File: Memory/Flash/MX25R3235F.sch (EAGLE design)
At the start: 2 parts, among them U2 MX25R3235FM1IH0

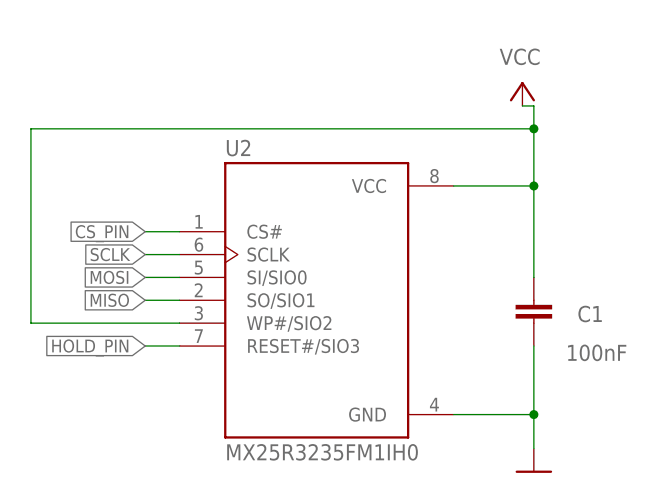
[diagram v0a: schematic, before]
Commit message: forder reordered and mx flash refactored
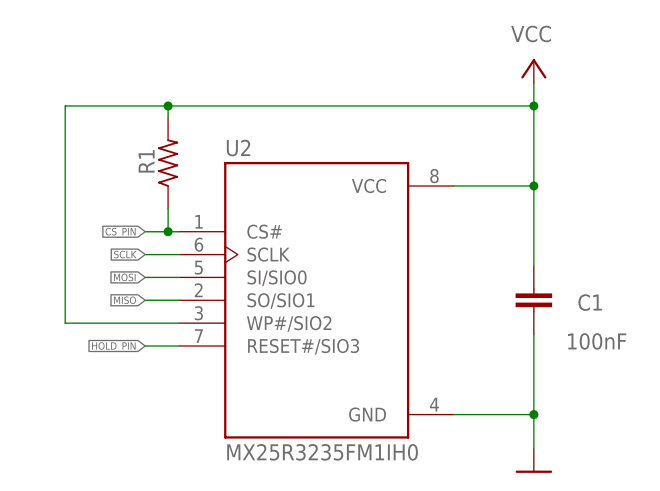
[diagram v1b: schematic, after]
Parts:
- added R1: (no value), rcl@1:R-US_R0603
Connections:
- net CS_PIN: now also R1.1
- net VCC: now also R1.2
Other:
- moved on the sheet: C1
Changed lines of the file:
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@@
 <?xml version="1.0" encoding="utf-8"?>
 <!DOCTYPE eagle SYSTEM "eagle.dtd">
-<eagle version="9.6.2">
+<eagle version="7.7.0">
 <drawing>
 <settings>
@@
 <part name="C1" library="rcl" deviceset="C-EU" device="C0603" value="100nF"/>
 <part name="GND1" library="supply1" deviceset="GND" device=""/>
+<part name="R1" library="rcl@1" deviceset="R-US_" device="R0603"/>
 </parts>
 <sheets>
@@
 <attribute name="VALUE" x="97.7894" y="41.909" size="1.7781" layer="96"/>
 </instance>
-<instance part="P+1" gate="VCC" x="130.81" y="83.82" smashed="yes" rot="MR0">
-<attribute name="VALUE" x="128.27" y="87.63" size="1.778" layer="96" rot="MR180"/>
-</instance>
-<instance part="C1" gate="G$1" x="132.08" y="57.15" smashed="yes" rot="R180">
-<attribute name="NAME" x="136.906" y="57.277" size="1.778" layer="95"/>
-<attribute name="VALUE" x="135.636" y="52.959" size="1.778" layer="96"/>
+<instance part="P+1" gate="VCC" x="132.08" y="86.36" smashed="yes" rot="MR0">
+<attribute name="VALUE" x="129.54" y="90.17" size="1.778" layer="96" rot="MR180"/>
+</instance>
+<instance part="C1" gate="G$1" x="132.08" y="58.42" smashed="yes" rot="R180">
+<attribute name="NAME" x="136.906" y="58.547" size="1.778" layer="95"/>
+<attribute name="VALUE" x="135.636" y="54.229" size="1.778" layer="96"/>
 </instance>
 <instance part="GND1" gate="1" x="132.08" y="40.64" smashed="yes"/>
+<instance part="R1" gate="G$1" x="91.44" y="74.93" smashed="yes" rot="R90">
+<attribute name="NAME" x="89.9414" y="73.66" size="1.778" layer="95" rot="R90"/>
+<attribute name="VALUE" x="94.742" y="71.12" size="1.778" layer="96" rot="R90"/>
+</instance>
 </instances>
 <busses>
@@
 <pinref part="C1" gate="G$1" pin="1"/>
 <wire x1="123.19" y1="46.99" x2="132.08" y2="46.99" width="0.1524" layer="91"/>
-<wire x1="132.08" y1="46.99" x2="132.08" y2="54.61" width="0.1524" layer="91"/>
+<wire x1="132.08" y1="46.99" x2="132.08" y2="55.88" width="0.1524" layer="91"/>
 <pinref part="U2" gate="G$1" pin="GND"/>
 <pinref part="GND1" gate="1" pin="GND"/>
@@
 <wire x1="123.19" y1="72.39" x2="132.08" y2="72.39" width="0.1524" layer="91"/>
 <pinref part="C1" gate="G$1" pin="2"/>
-<wire x1="132.08" y1="72.39" x2="132.08" y2="62.23" width="0.1524" layer="91"/>
+<wire x1="132.08" y1="72.39" x2="132.08" y2="63.5" width="0.1524" layer="91"/>
 <pinref part="P+1" gate="VCC" pin="VCC"/>
-<wire x1="130.81" y1="81.28" x2="132.08" y2="81.28" width="0.1524" layer="91"/>
-<wire x1="132.08" y1="81.28" x2="132.08" y2="78.74" width="0.1524" layer="91"/>
+<wire x1="132.08" y1="83.82" x2="132.08" y2="81.28" width="0.1524" layer="91"/>
 <junction x="132.08" y="72.39"/>
 <pinref part="U2" gate="G$1" pin="WP#/SIO2"/>
-<wire x1="132.08" y1="78.74" x2="132.08" y2="72.39" width="0.1524" layer="91"/>
-<wire x1="92.71" y1="57.15" x2="76.2" y2="57.15" width="0.1524" layer="91"/>
-<wire x1="76.2" y1="57.15" x2="76.2" y2="78.74" width="0.1524" layer="91"/>
-<wire x1="76.2" y1="78.74" x2="132.08" y2="78.74" width="0.1524" layer="91"/>
-<junction x="132.08" y="78.74"/>
+<wire x1="132.08" y1="81.28" x2="132.08" y2="72.39" width="0.1524" layer="91"/>
+<wire x1="92.71" y1="57.15" x2="80.01" y2="57.15" width="0.1524" layer="91"/>
+<wire x1="80.01" y1="57.15" x2="80.01" y2="81.28" width="0.1524" layer="91"/>
+<wire x1="80.01" y1="81.28" x2="91.44" y2="81.28" width="0.1524" layer="91"/>
+<junction x="132.08" y="81.28"/>
+<pinref part="R1" gate="G$1" pin="2"/>
+<wire x1="91.44" y1="81.28" x2="132.08" y2="81.28" width="0.1524" layer="91"/>
+<wire x1="91.44" y1="80.01" x2="91.44" y2="81.28" width="0.1524" layer="91"/>
+<junction x="91.44" y="81.28"/>
 </segment>
 </net>
@@
 <segment>
 <pinref part="U2" gate="G$1" pin="CS#"/>
-<wire x1="92.71" y1="67.31" x2="88.9" y2="67.31" width="0.1524" layer="91"/>
-<label x="88.9" y="67.31" size="1.4224" layer="95" rot="R180" xref="yes"/>
+<wire x1="92.71" y1="67.31" x2="91.44" y2="67.31" width="0.1524" layer="91"/>
+<label x="88.9" y="67.31" size="0.8128" layer="95" rot="R180" xref="yes"/>
+<pinref part="R1" gate="G$1" pin="1"/>
+<wire x1="91.44" y1="67.31" x2="88.9" y2="67.31" width="0.1524" layer="91"/>
+<wire x1="91.44" y1="69.85" x2="91.44" y2="67.31" width="0.1524" layer="91"/>
+<junction x="91.44" y="67.31"/>
 </segment>
 </net>
@@
 <pinref part="U2" gate="G$1" pin="SCLK"/>
 <wire x1="92.71" y1="64.77" x2="88.9" y2="64.77" width="0.1524" layer="91"/>
-<label x="88.9" y="64.77" size="1.4224" layer="95" rot="R180" xref="yes"/>
+<label x="88.9" y="64.77" size="0.8128" layer="95" rot="R180" xref="yes"/>
 </segment>
 </net>
@@
 <pinref part="U2" gate="G$1" pin="SI/SIO0"/>
 <wire x1="92.71" y1="62.23" x2="88.9" y2="62.23" width="0.1524" layer="91"/>
-<label x="88.9" y="62.23" size="1.4224" layer="95" rot="R180" xref="yes"/>
+<label x="88.9" y="62.23" size="0.8128" layer="95" rot="R180" xref="yes"/>
 </segment>
 </net>
@@
 <pinref part="U2" gate="G$1" pin="SO/SIO1"/>
 <wire x1="92.71" y1="59.69" x2="88.9" y2="59.69" width="0.1524" layer="91"/>
-<label x="88.9" y="59.69" size="1.4224" layer="95" rot="R180" xref="yes"/>
+<label x="88.9" y="59.69" size="0.8128" layer="95" rot="R180" xref="yes"/>
 </segment>
 </net>
@@
 <pinref part="U2" gate="G$1" pin="RESET#/SIO3"/>
 <wire x1="92.71" y1="54.61" x2="88.9" y2="54.61" width="0.1524" layer="91"/>
-<label x="88.9" y="54.61" size="1.4224" layer="95" rot="R180" xref="yes"/>
-</segment>
-</net>
+<label x="88.9" y="54.61" size="0.8128" layer="95" rot="R180" xref="yes"/>
+</segment>
+</net>
